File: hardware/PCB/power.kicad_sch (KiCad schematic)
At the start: 67 parts

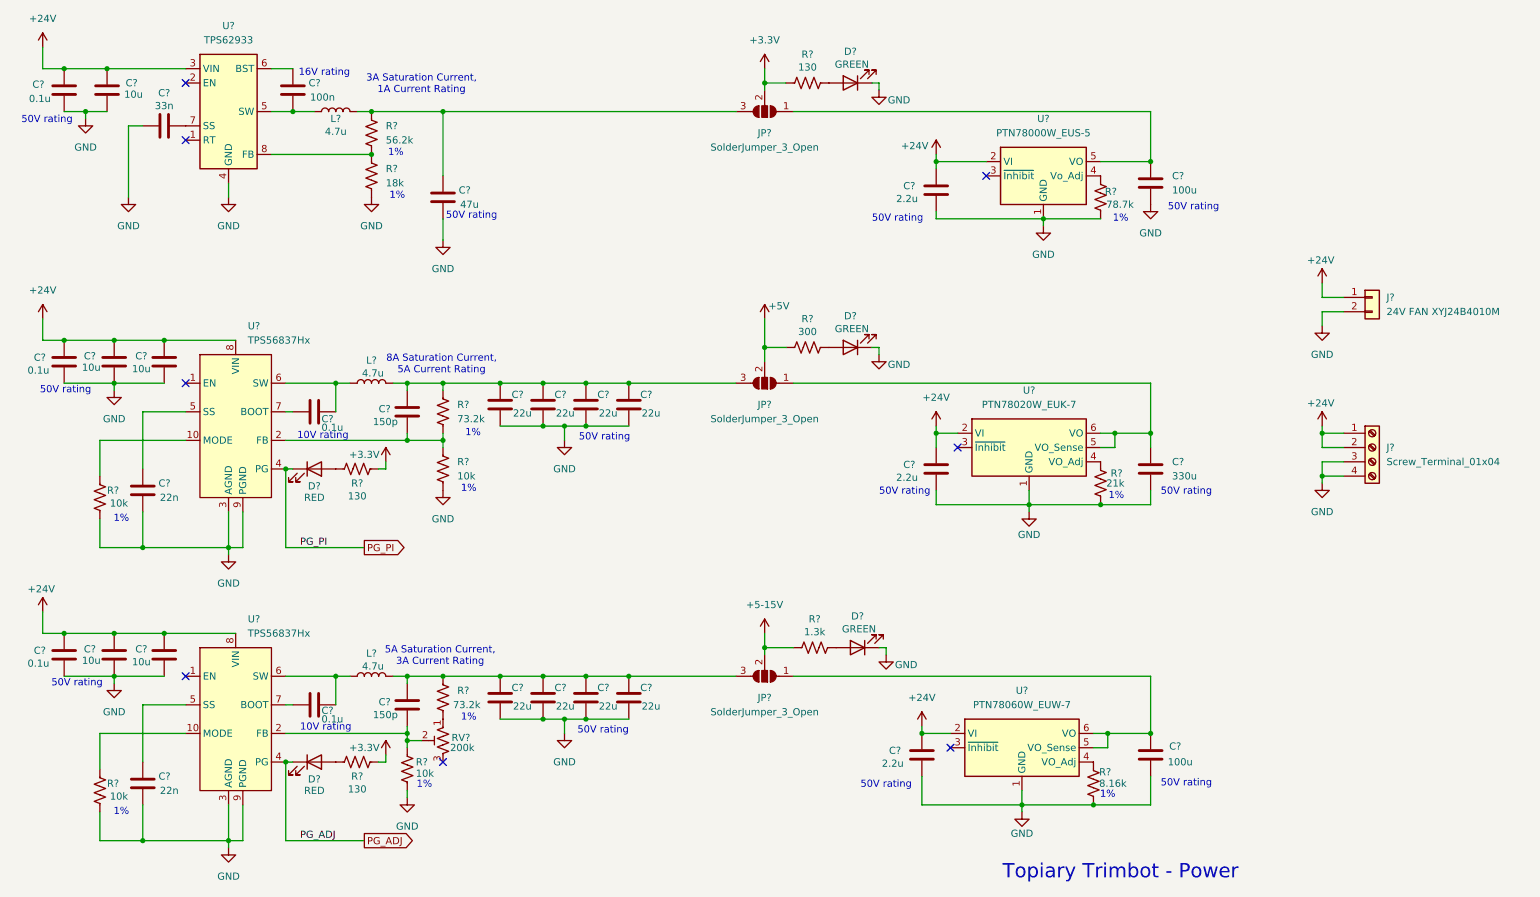
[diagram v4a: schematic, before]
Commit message: Schematic - Power Components and Footprints
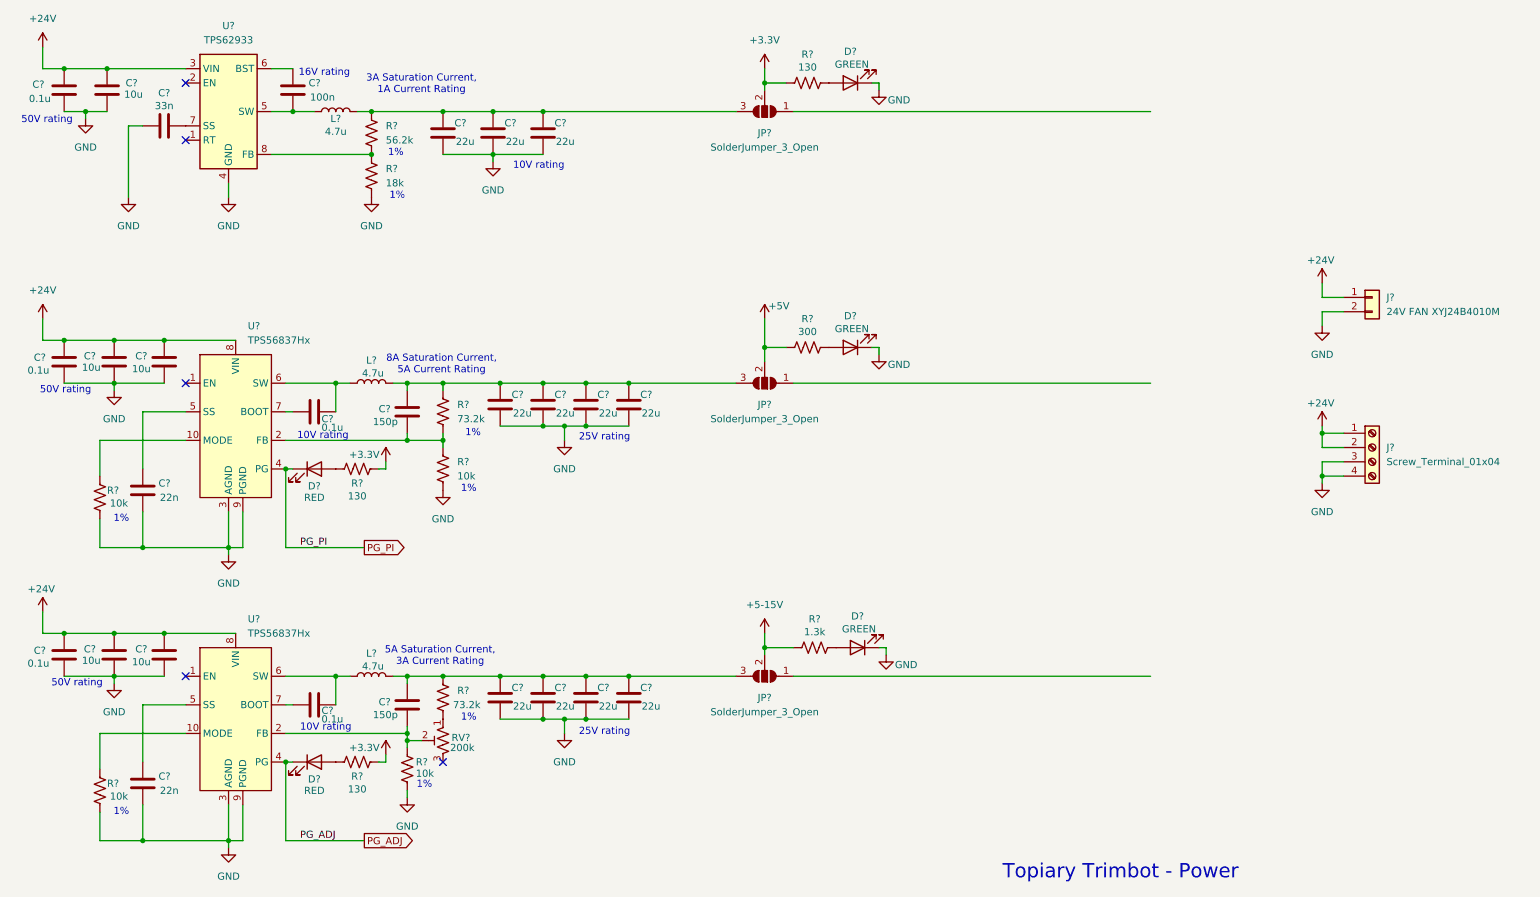
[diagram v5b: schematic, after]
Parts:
- removed C? (x3): 2.2u, symbol Device:C
- removed C? (x2): 100u, symbol Device:C
- removed C?: 330u, symbol Device:C
- removed C?: 47u, symbol Device:C
- removed R?: 21k, Resistor_SMD:R_0805_2012Metric, symbol Device:R_US
- removed R?: 8.16k, Resistor_SMD:R_0805_2012Metric, symbol Device:R_US
- removed R?: 78.7k, Resistor_SMD:R_0805_2012Metric, symbol Device:R_US
- removed U?: PTN78020W_EUK-7, Module:Texas_EUK_R-PDSS-T7_THT, symbol Converter_DCDC:PTN78020W_EUK-7
- removed U?: PTN78000W_EUS-5, Module:Texas_EUS_R-PDSS-T5_THT, symbol Converter_DCDC:PTN78000W_EUS-5
- removed U?: PTN78060W_EUW-7, Module:Texas_EUW_R-PDSS-T7_THT, symbol Converter_DCDC:PTN78060W_EUW-7
- added C? (x3): 22u, Capacitor_SMD:C_0805_2012Metric, symbol Device:C
- C? (x6): footprint (none) -> Capacitor_SMD:C_0805_2012Metric
- C? (x5): footprint (none) -> Capacitor_SMD:C_0805_2012Metric; MANUFACTURER (none) -> Murata Electronics; Manufacturer_Part_Number (none) -> GRM21BR61H106KE43L
- C? (x8): footprint (none) -> Capacitor_SMD:C_0805_2012Metric; MANUFACTURER (none) -> Murata Electronics; Manufacturer_Part_Number (none) -> GRM21BR61E226ME44L
- C? (x5): footprint (none) -> Capacitor_SMD:C_0805_2012Metric; MANUFACTURER (none) -> KEMET; Manufacturer_Part_Number (none) -> C0805C104K5RACTU
- L?: MANUFACTURER (none) -> Bourns; Manufacturer_Part_Number (none) -> SRP3220A-4R7M
- L?: MANUFACTURER (none) -> Eaton; Manufacturer_Part_Number (none) -> HCP0704-4R7-R
- L?: MANUFACTURER (none) -> Bourns; Manufacturer_Part_Number (none) -> SRP5020CC-4R7M
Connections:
- net GND: now also C?.2, C?.2, C?.2
- net at JP?.3 (B), L?.2, R?.1: now also C?.1, C?.1, C?.1
- no-connect marks 8 -> 5
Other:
- note added: "25V rating"

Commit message: Schematic - New Power Modules
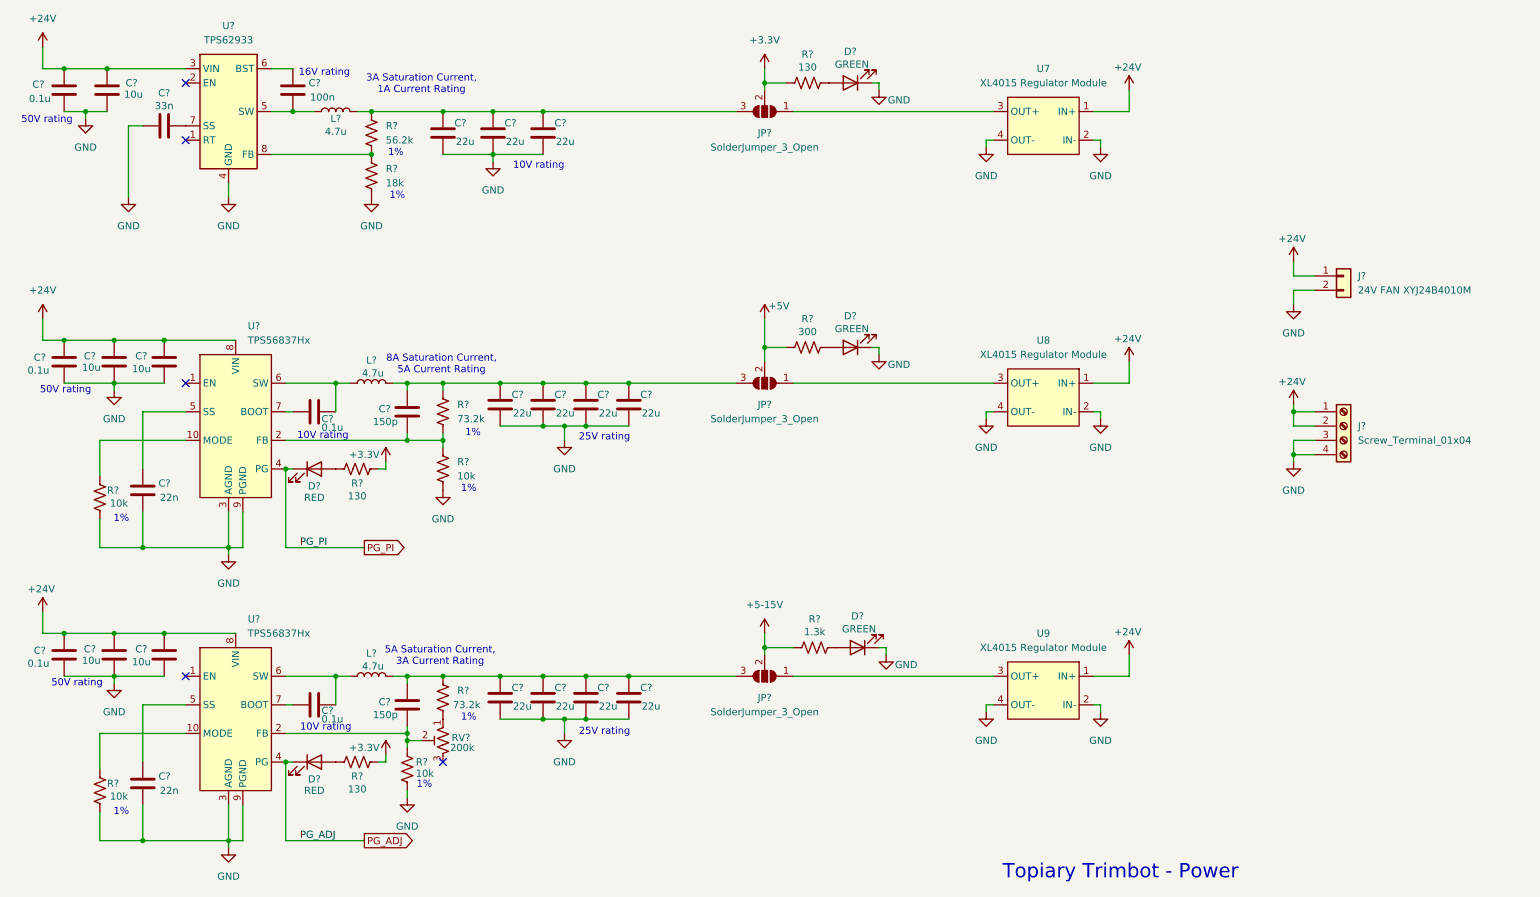
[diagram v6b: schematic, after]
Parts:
- added U7, U8, U9: XL4015 Regulator Module, CustomFootprints:XL4015_Regulator_Module, symbol CustomSymbols:XL4015_Regulator_Module
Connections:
- net +24V: now also U7.1 (IN+), U8.1 (IN+), U9.1 (IN+)
- net GND: now also U7.2 (IN-), U7.4 (OUT-), U8.2 (IN-), U8.4 (OUT-), U9.2 (IN-), U9.4 (OUT-)
- net at JP?.1 (A): now also U9.3 (OUT+)
- net at JP?.1 (A): now also U7.3 (OUT+)
- net at JP?.1 (A): now also U8.3 (OUT+)
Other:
- moved on the sheet: J?

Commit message: Synchronized schematic draft and reannotated all
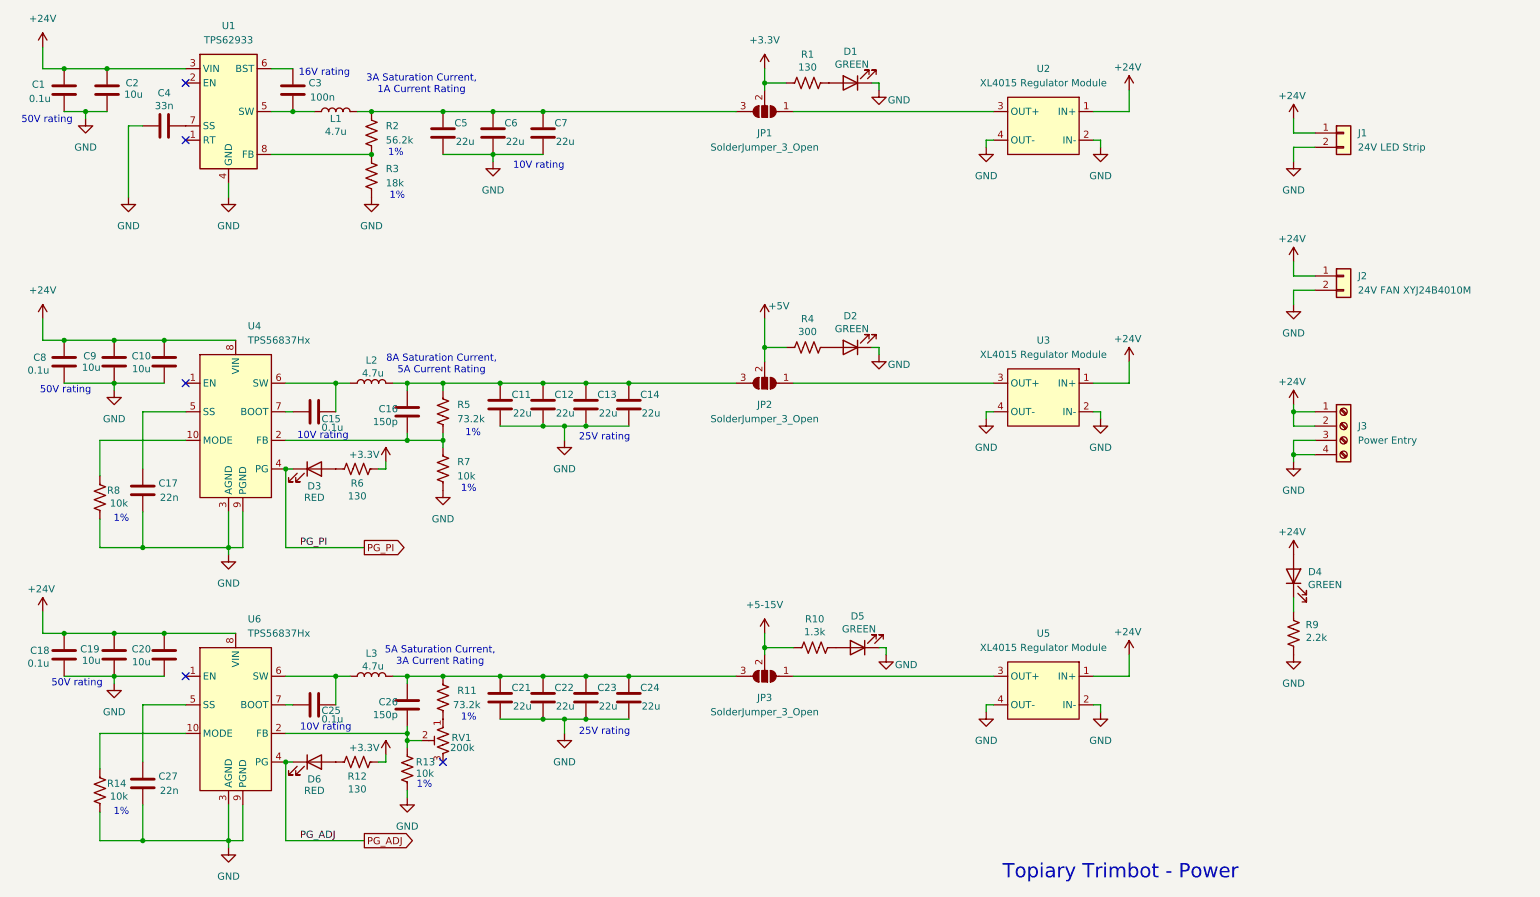
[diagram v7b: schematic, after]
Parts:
- added D4: GREEN, LED_SMD:LED_0805_2012Metric, symbol Device:LED
- added J1: 24V LED Strip, Connector_Molex:Molex_KK-254_AE-6410-02A_1x02_P2.54mm_Vertical, symbol Connector_Generic:Conn_01x02
- added R9: 2.2k, Resistor_SMD:R_0805_2012Metric, symbol Device:R_US
- C5, C6, C7: renamed from C?; Manufacturer_Part_Number GRM21BZ71A226ME15L -> GRM21BR61E226ME44L
- J3: renamed from J?; value Screw_Terminal_01x04 -> Power Entry
- JP1, JP2, JP3: renamed from JP?; footprint (none) -> Jumper:SolderJumper-3_P2.0mm_Open_TrianglePad1.0x1.5mm
- L1: renamed from L?; footprint (none) -> Inductor_SMD:L_TDK_VLS6045EX_VLS6045AF; MANUFACTURER Bourns -> TDK; Manufacturer_Part_Number SRP3220A-4R7M -> VLS6045EX-4R7M
- L2: renamed from L?; footprint (none) -> Inductor_SMD:L_APV_APH1050; MANUFACTURER Eaton -> Laird; Manufacturer_Part_Number HCP0704-4R7-R -> MGAH10044R7M-10
- L3: renamed from L?; footprint (none) -> Inductor_SMD:L_APV_APH1050; MANUFACTURER Bourns -> Laird; Manufacturer_Part_Number SRP5020CC-4R7M -> MGAH10044R7M-10
- gave numbers to parts that had none: 47
- renumbered U7 to U2, U8 to U3, U9 to U5
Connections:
- net +24V: now also D4.2 (A), J1.1 (Pin_1)
- net GND: now also J1.2 (Pin_2), R9.2
- new net: D4.1 (K), R9.1

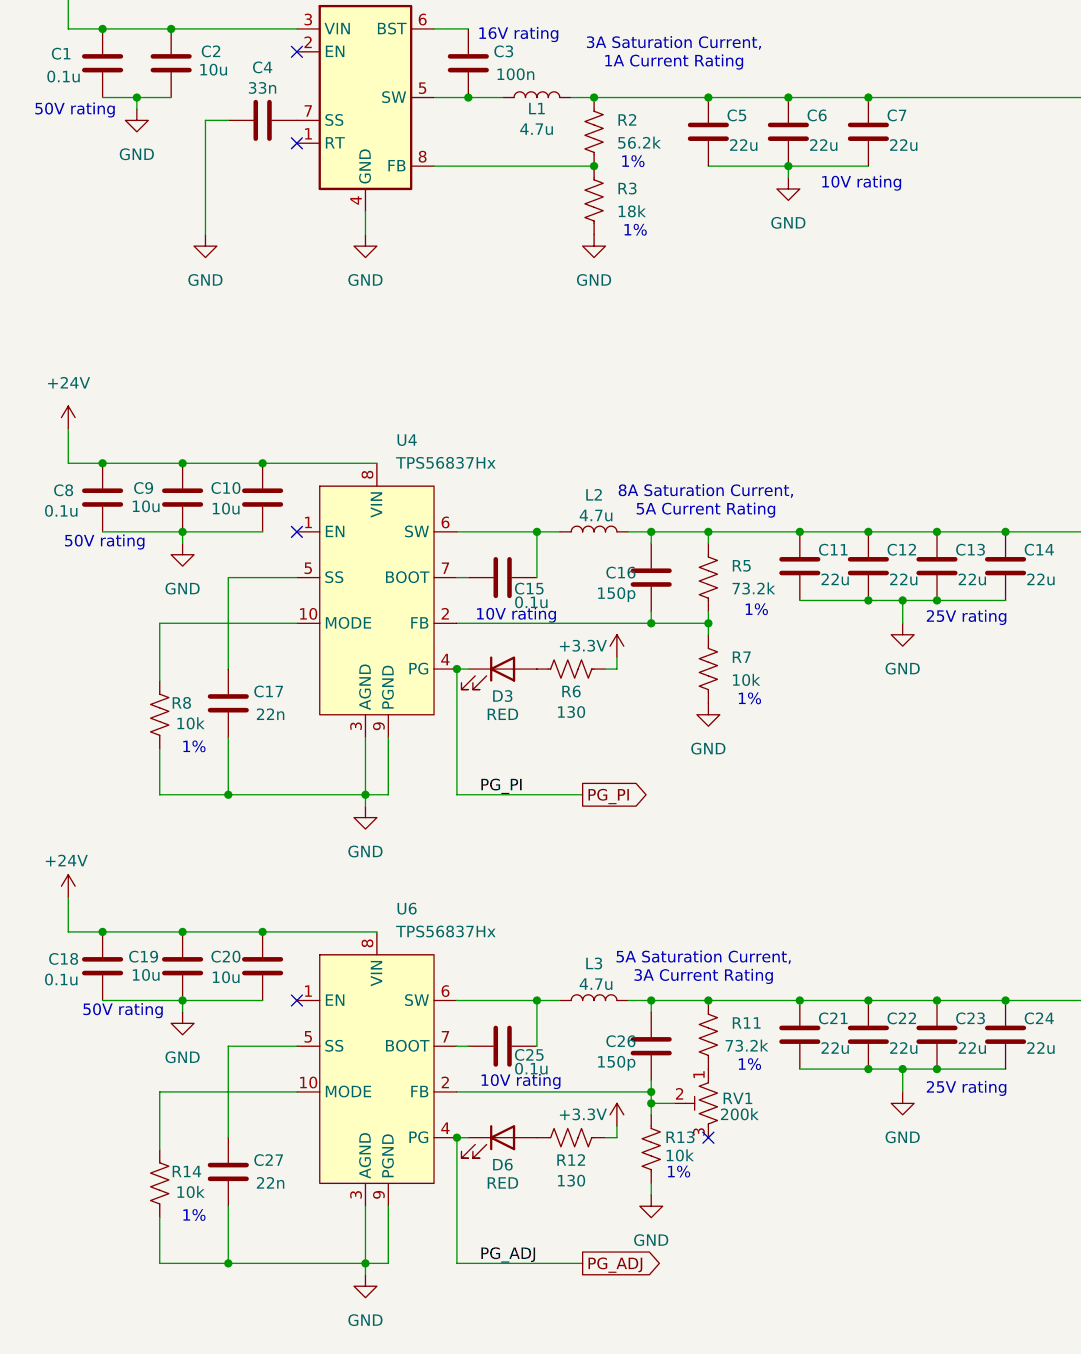
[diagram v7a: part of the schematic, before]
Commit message: Add components to PCB, fix some ERC violations
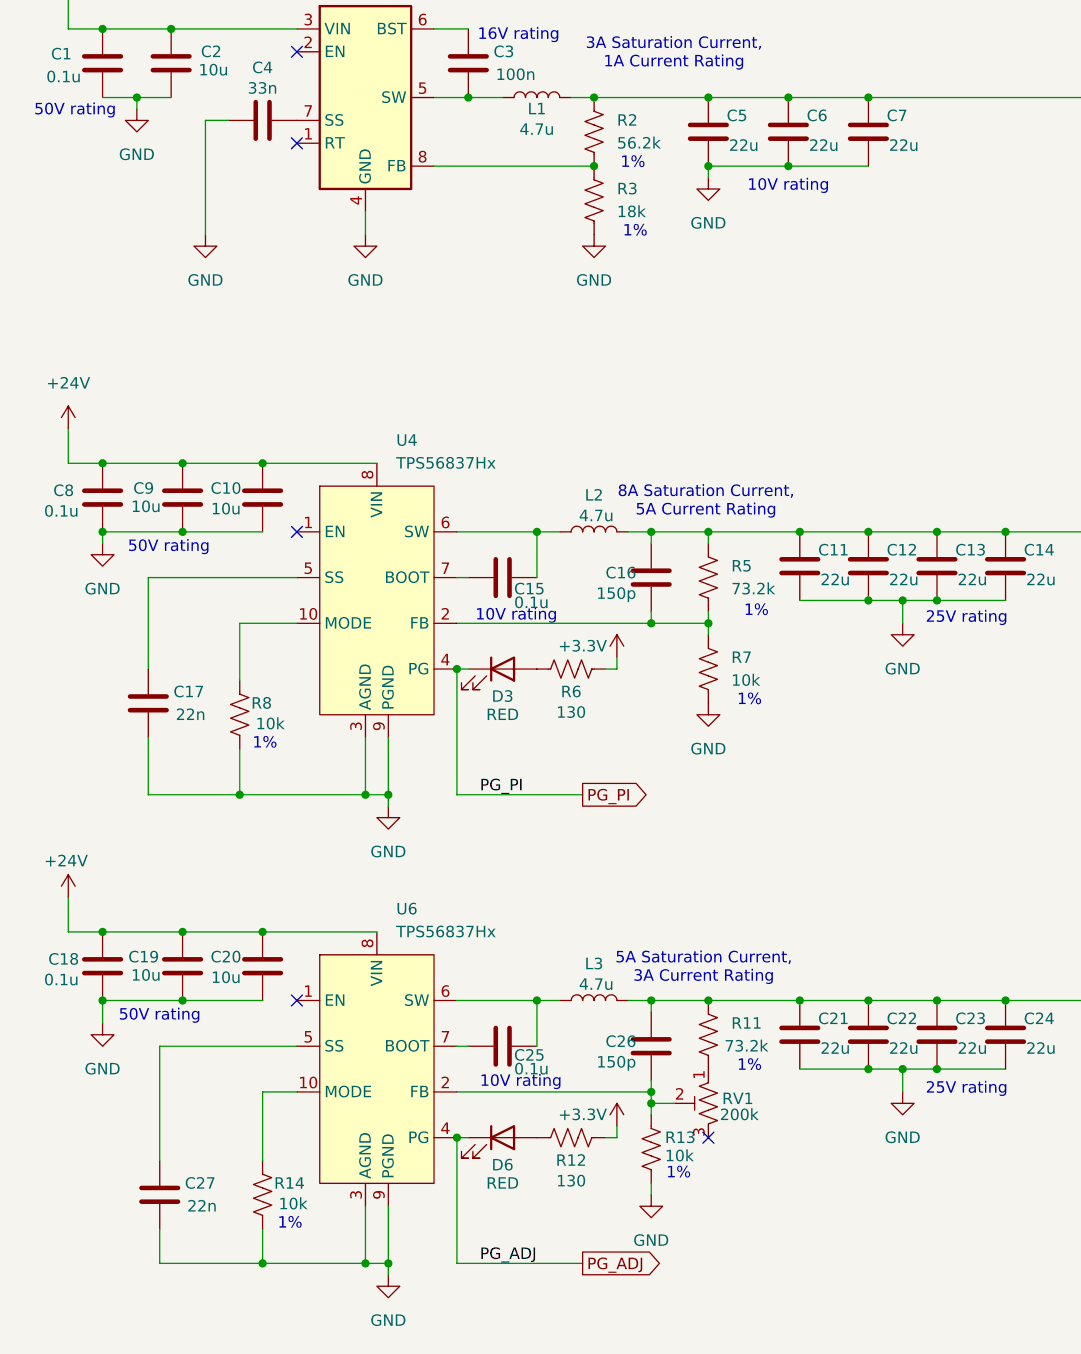
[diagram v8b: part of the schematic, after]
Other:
- moved on the sheet: C17, C27, R14, R8
